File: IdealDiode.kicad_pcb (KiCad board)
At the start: 2 copper layers, 13.7 x 9.1 mm, 11 parts, among them J1 Conn_01x01_Pin, J2 Conn_01x01_Pin, J3 Conn_01x01_Pin, J4 Conn_01x01_Pin, Q1 AO3400A, Q2 AO3401A, U1 LM393

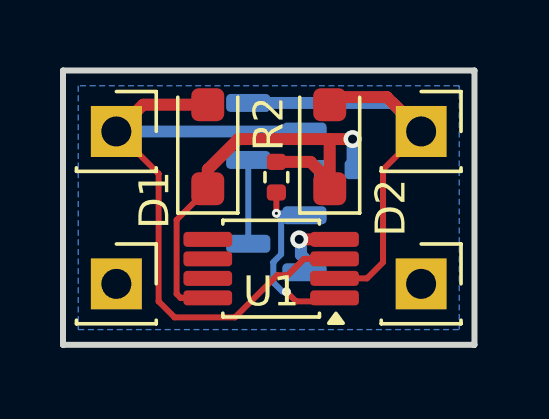
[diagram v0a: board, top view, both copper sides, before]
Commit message: Fixed wrong footprint issue
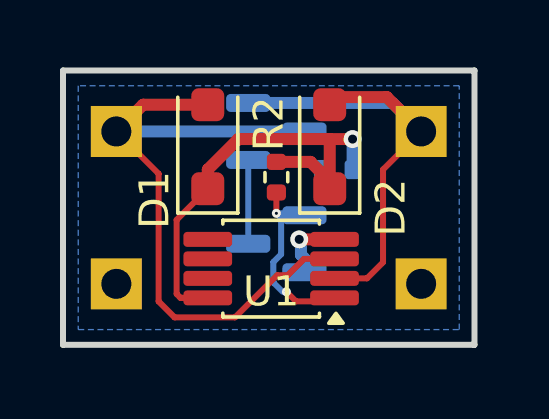
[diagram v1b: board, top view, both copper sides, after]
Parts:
- J1, J2, J3, J4: footprint Connector_PinSocket_2.54mm:PinSocket_1x01_P2.54mm_Vertical -> Connector_PinHeader_2.54mm:PinHeader_1x01_P2.54mm_Vertical; moved to B.Cu
- turned J1 to 180 degrees
- turned J2 to 180 degrees
- turned J3 to 180 degrees
- turned J4 to 180 degrees

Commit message: Modified the design to be single-sided, prepared for PCBA at JLCPCB
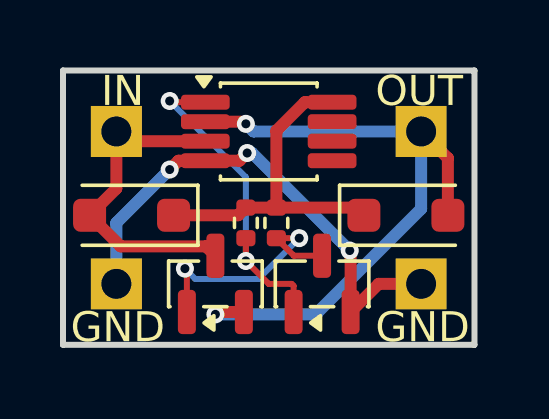
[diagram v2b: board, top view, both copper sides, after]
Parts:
- Q1, Q2, R1: moved to F.Cu
- moved Q2 5.47 mm to (102.4, 101.6), turned to 90 degrees
- moved U1 4.57 mm to (104.1, 96.5), turned to 0 degrees
- moved D1 3.42 mm to (99.6, 99.3), turned to 180 degrees
- moved D2 3.42 mm to (108.7, 99.3), turned to 0 degrees
- moved R1 2.70 mm to (104.4, 99.6), turned to 90 degrees
- moved Q1 2.03 mm to (105.9, 101.6), turned to 90 degrees
- moved R2 1.83 mm to (103.4, 99.6)
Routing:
- net GND: track 2.35 -> 16.9 mm, vias 1 -> 3
- net /i: track 23.4 -> 11.0 mm
- net /o: track 16.4 -> 22.4 mm, vias 0 -> 2
- net Net-(Q1-G): track 6.36 -> 11.2 mm
- net /a: track 15.6 -> 11.4 mm, vias 1 -> 0
- net Net-(Q1-D): track 5.39 -> 8.52 mm, vias 0 -> 2
- removed copper zone on B.Cu, net GND
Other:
- board text added: "GND"
- board text added: "IN"
- board text added: "OUT"
